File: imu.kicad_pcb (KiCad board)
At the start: 2 copper layers, 32.3 x 28.4 mm, 21 parts, among them J1 Conn_01x06, U1 LSM6DSL, U2 LIS2MDL, U3 AMS1117-3.3

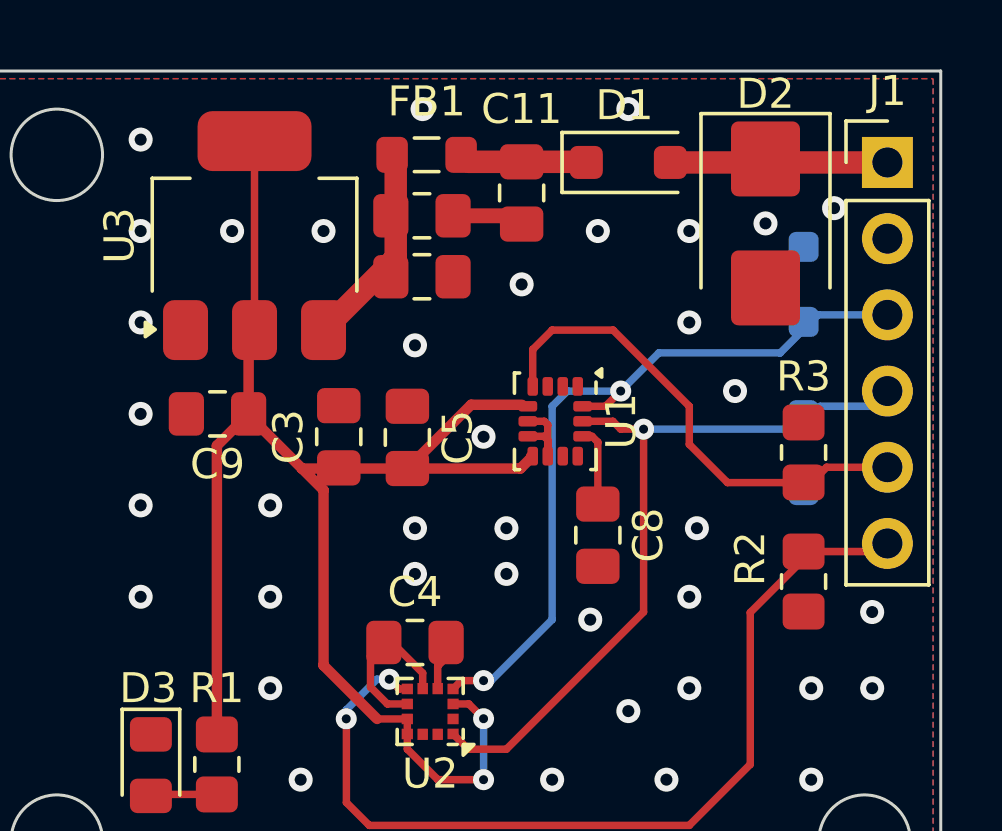
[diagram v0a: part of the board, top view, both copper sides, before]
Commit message: Add Fabrication Outputs
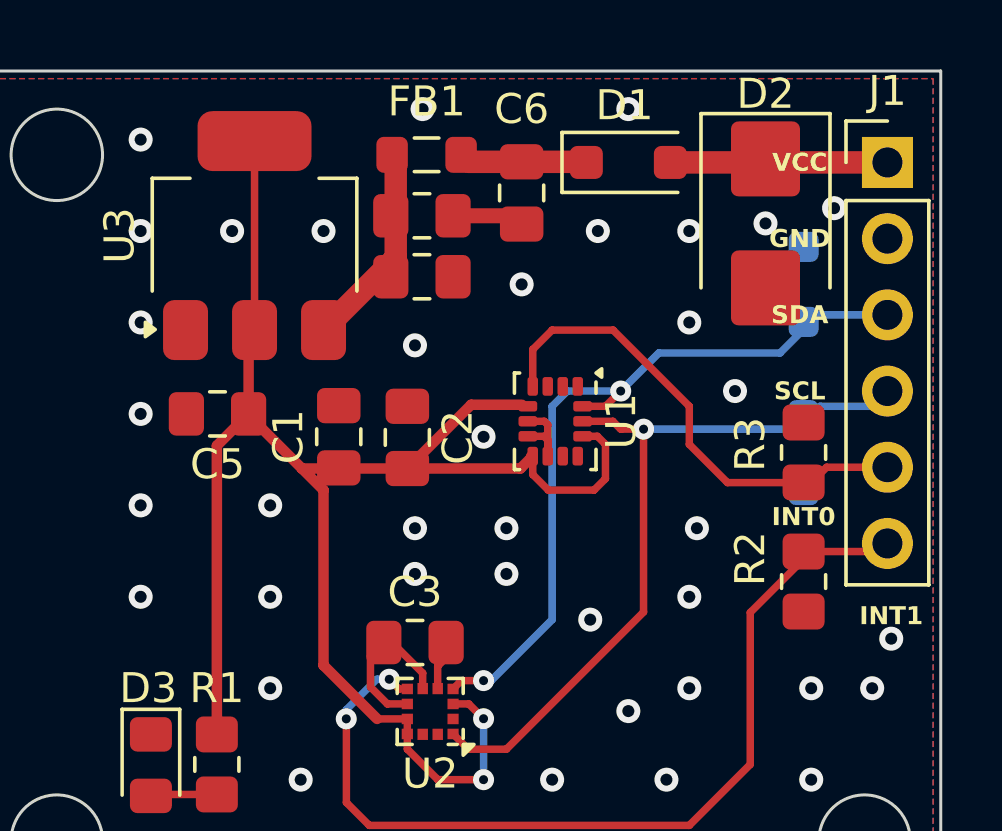
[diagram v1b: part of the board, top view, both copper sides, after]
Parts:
- removed C8: 200nF, Capacitor_SMD:C_0805_2012Metric_Pad1.18x1.45mm_HandSolder
- C3: renamed from C4; value 200nF -> 220nF
- renumbered C3 to C1, C5 to C2, C10 to C4, C9 to C5, C11 to C6, C12 to C7
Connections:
- U1 pad 12: Net-(U1-CS) -> +3V3
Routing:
- net +3V3: track 52.7 -> 58.2 mm
- net Net-(U1-CS): track 2.65 -> 0.00 mm
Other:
- board text added: "GND"
- board text added: "INT0"
- board text added: "INT1"
- board text added: "SCL"
- board text added: "SDA"
- board text added: "VCC"

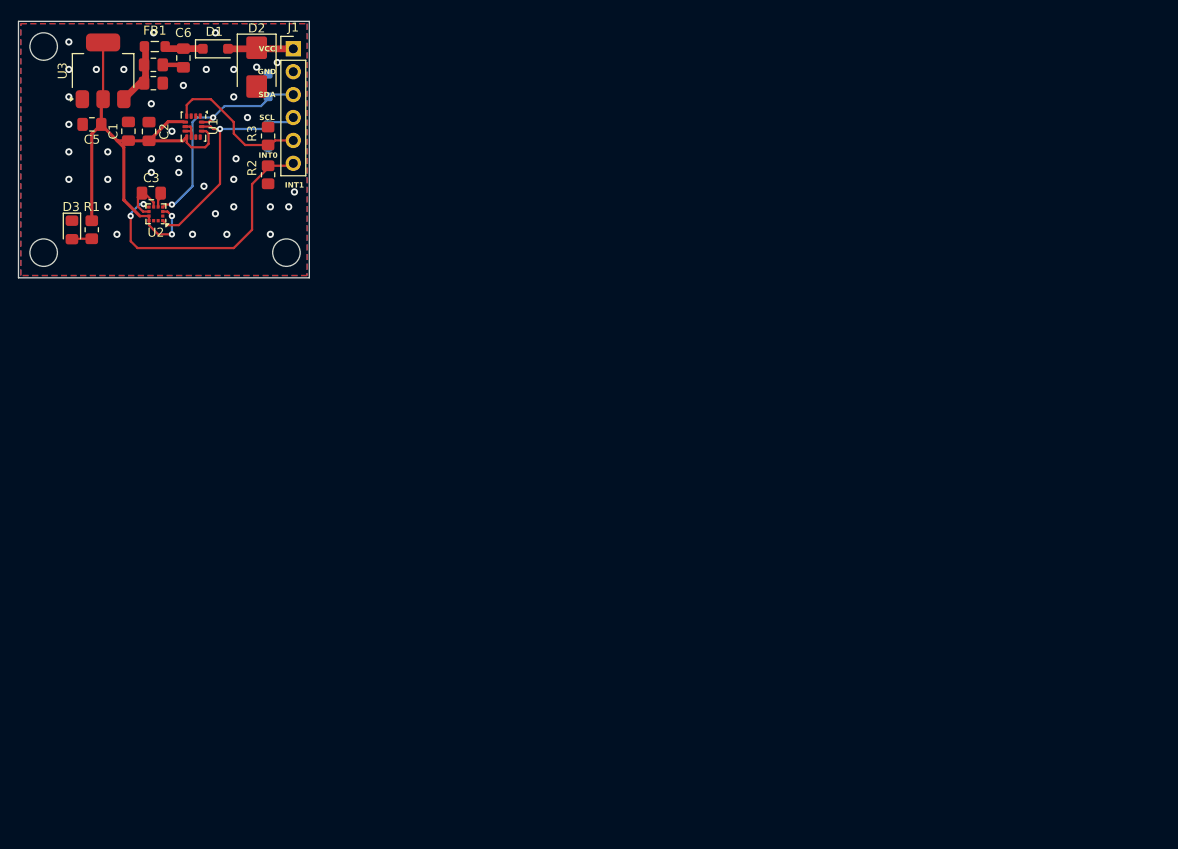
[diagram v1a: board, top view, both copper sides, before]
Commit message: Add Hierarchal Schematic + JST Connectors + GPIO
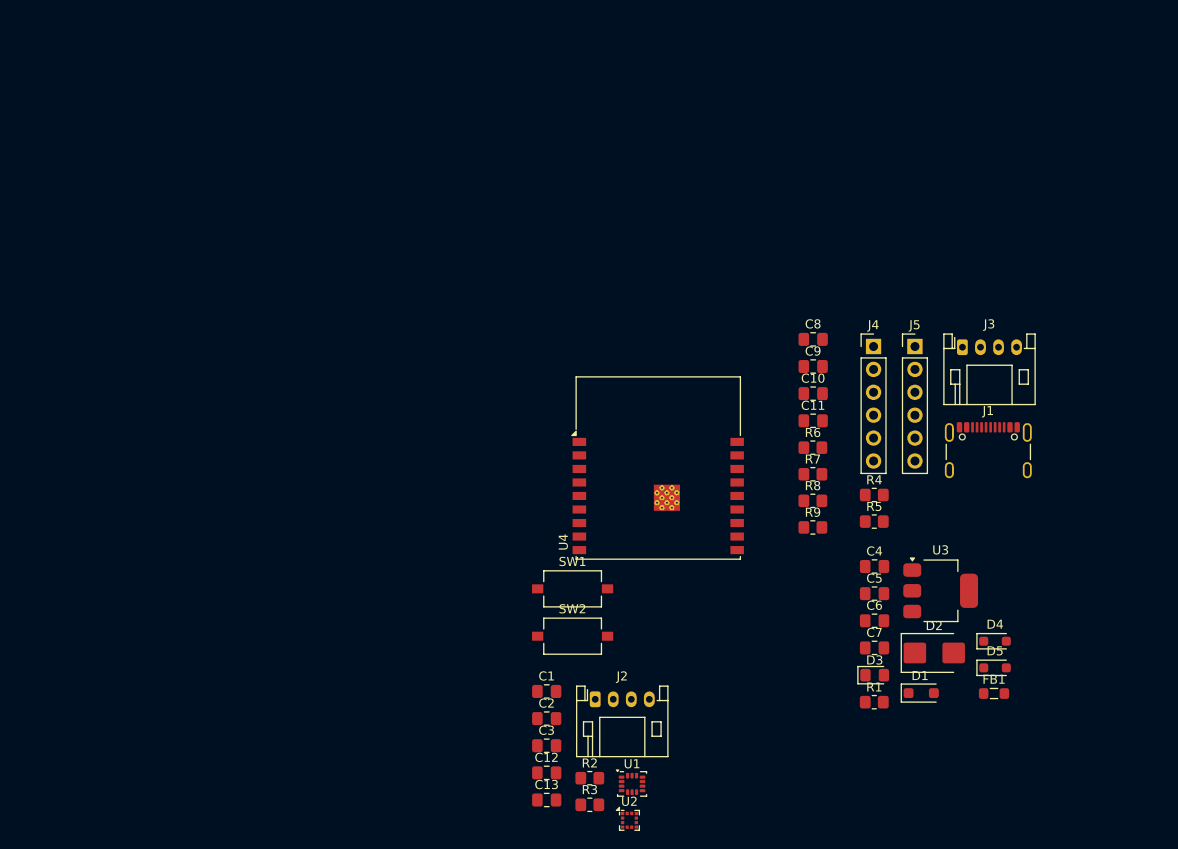
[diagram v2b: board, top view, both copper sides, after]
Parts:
- added C10: 1uF, Capacitor_SMD:C_0805_2012Metric_Pad1.18x1.45mm_HandSolder, F.Cu at (147.6, 60.1)
- added C11: 100nF, Capacitor_SMD:C_0805_2012Metric_Pad1.18x1.45mm_HandSolder, F.Cu at (147.6, 63.1)
- added C12: 10uF, Capacitor_SMD:C_0805_2012Metric_Pad1.18x1.45mm_HandSolder, F.Cu at (118.0, 102.2)
- added C13: 100nF, Capacitor_SMD:C_0805_2012Metric_Pad1.18x1.45mm_HandSolder, F.Cu at (118.0, 105.2)
- added C8: 100nF, Capacitor_SMD:C_0805_2012Metric_Pad1.18x1.45mm_HandSolder, F.Cu at (147.6, 54.1)
- added C9: 22uF, Capacitor_SMD:C_0805_2012Metric_Pad1.18x1.45mm_HandSolder, F.Cu at (147.6, 57.1)
- added J2: JST_PH2.0_01x04, Connector_JST:JST_PH_S4B-PH-K_1x04_P2.00mm_Horizontal, F.Cu at (123.4, 94.0)
- added J3: JST_PH2.0_01x04, Connector_JST:JST_PH_S4B-PH-K_1x04_P2.00mm_Horizontal, F.Cu at (164.1, 54.9)
- added J4: GPIO0, Connector_PinHeader_2.54mm:PinHeader_1x06_P2.54mm_Vertical, F.Cu at (154.3, 54.9)
- added J5: GPIO1, Connector_PinHeader_2.54mm:PinHeader_1x06_P2.54mm_Vertical, F.Cu at (158.9, 54.9)
- added R4: 5.1kR, Resistor_SMD:R_0805_2012Metric_Pad1.20x1.40mm_HandSolder, F.Cu at (154.4, 71.3)
- added R5: 5.1kR, Resistor_SMD:R_0805_2012Metric_Pad1.20x1.40mm_HandSolder, F.Cu at (154.4, 74.3)
- added R6: 10kR, Resistor_SMD:R_0805_2012Metric_Pad1.20x1.40mm_HandSolder, F.Cu at (147.5, 66.1)
- added R7: 100R, Resistor_SMD:R_0805_2012Metric_Pad1.20x1.40mm_HandSolder, F.Cu at (147.5, 69.0)
- added R8: 2.2kR, Resistor_SMD:R_0805_2012Metric_Pad1.20x1.40mm_HandSolder, F.Cu at (147.5, 72.0)
- added R9: 2.2kR, Resistor_SMD:R_0805_2012Metric_Pad1.20x1.40mm_HandSolder, F.Cu at (147.5, 74.9)
- added SW1: SW_Push, Button_Switch_SMD:SW_Tactile_SPST_NO_Straight_CK_PTS636Sx25SMTRLFS, F.Cu at (120.9, 81.7)
- added SW2: SW_Push, Button_Switch_SMD:SW_Tactile_SPST_NO_Straight_CK_PTS636Sx25SMTRLFS, F.Cu at (120.9, 87.0)
- added U4: ESP32-C3-WROOM-02, RF_Module:ESP32-C3-WROOM-02, F.Cu at (130.4, 71.4)
- D4, D5: moved to F.Cu
- J1: value Conn_01x06 -> USB_C_Receptacle_USB2.0_16P; footprint Connector_PinHeader_2.54mm:PinHeader_1x06_P2.54mm_Vertical -> Connector_USB:USB_C_Receptacle_GCT_USB4105-xx-A_16P_TopMnt_Horizontal
- moved FB1 117.5 mm to (167.6, 93.3), turned to 0 degrees
- moved U3 109.3 mm to (161.7, 82.0), turned to 0 degrees
- moved D1 106.0 mm to (159.6, 93.3)
- moved D5 103.3 mm to (167.8, 90.5), turned to 0 degrees
- moved C7 102.9 mm to (154.4, 88.3), turned to 0 degrees
- moved D3 101.8 mm to (154.4, 91.3), turned to 0 degrees
- moved R1 101.4 mm to (154.4, 94.3), turned to 0 degrees
- moved C5 101.2 mm to (154.4, 82.3), turned to 0 degrees
- moved D2 99.3 mm to (161.0, 88.8), turned to 0 degrees
- moved C6 98.9 mm to (154.4, 85.3), turned to 0 degrees
- moved D4 98.2 mm to (167.8, 87.5), turned to 0 degrees
- moved C4 96.3 mm to (154.4, 79.3)
- moved J1 89.6 mm to (167.0, 67.5)
- moved U1 87.6 mm to (127.5, 103.4), turned to 0 degrees
- moved U2 85.3 mm to (127.2, 107.4), turned to 0 degrees
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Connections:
- C4 pad 1: VCC -> +5V
- C7 pad 2: VCC -> +5V
- D1 pad 2: Net-(D1-A) -> +5V
- D2 pad 1: Net-(D1-A) -> GND
- D2 pad 2: GND -> +5V
- D5 pad 2: SDA -> SCL
- FB1 pad 2: VCC -> +5V
- R2 pad 1: INT1 -> INT_MAG
- R3 pad 1: INT0 -> INT_IMU
- U1 pad 14: SDA -> SCL
- U1 pad 4: INT0 -> INT_IMU
- U2 pad 4: SDA -> SCL
- U2 pad 7: INT1 -> INT_MAG
- U3 pad 3: VCC -> +5V
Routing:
- net +3V3: track 58.2 -> 0.00 mm, vias 2 -> 0
- net INT1: track 30.9 -> 0.00 mm, vias 2 -> 0
- net SCL: track 25.3 -> 0.00 mm, vias 1 -> 0
- net SDA: track 25.3 -> 0.00 mm, vias 2 -> 0
- net INT0: track 16.4 -> 0.00 mm
- net GND: track 10.2 -> 0.00 mm, vias 38 -> 0
- net Net-(D1-A): track 7.24 -> 0.00 mm
- net VCC: track 6.58 -> 0.00 mm
- net Net-(D1-K): track 4.28 -> 0.00 mm
- net Net-(D3-A): track 2.22 -> 0.00 mm
- net Net-(U2-C1): track 1.65 -> 0.00 mm
- removed copper zone on B.Cu, net GND
- removed copper zone on F.Cu, net GND
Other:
- board outline removed
- board text removed: "GND"
- board text removed: "INT0"
- board text removed: "INT1"
- board text removed: "SCL"
- board text removed: "SDA"
- board text removed: "VCC"

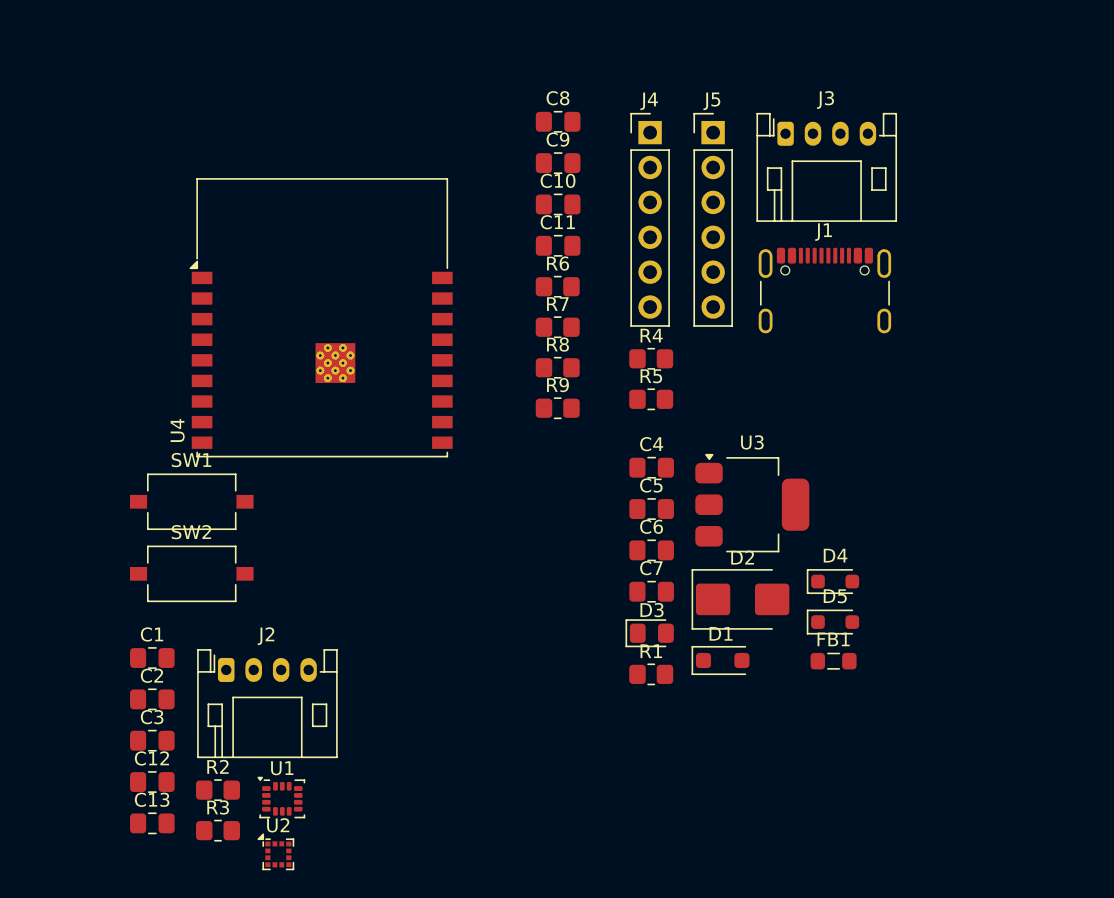
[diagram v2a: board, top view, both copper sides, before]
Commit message: Route Traces for ESP32 and related IO
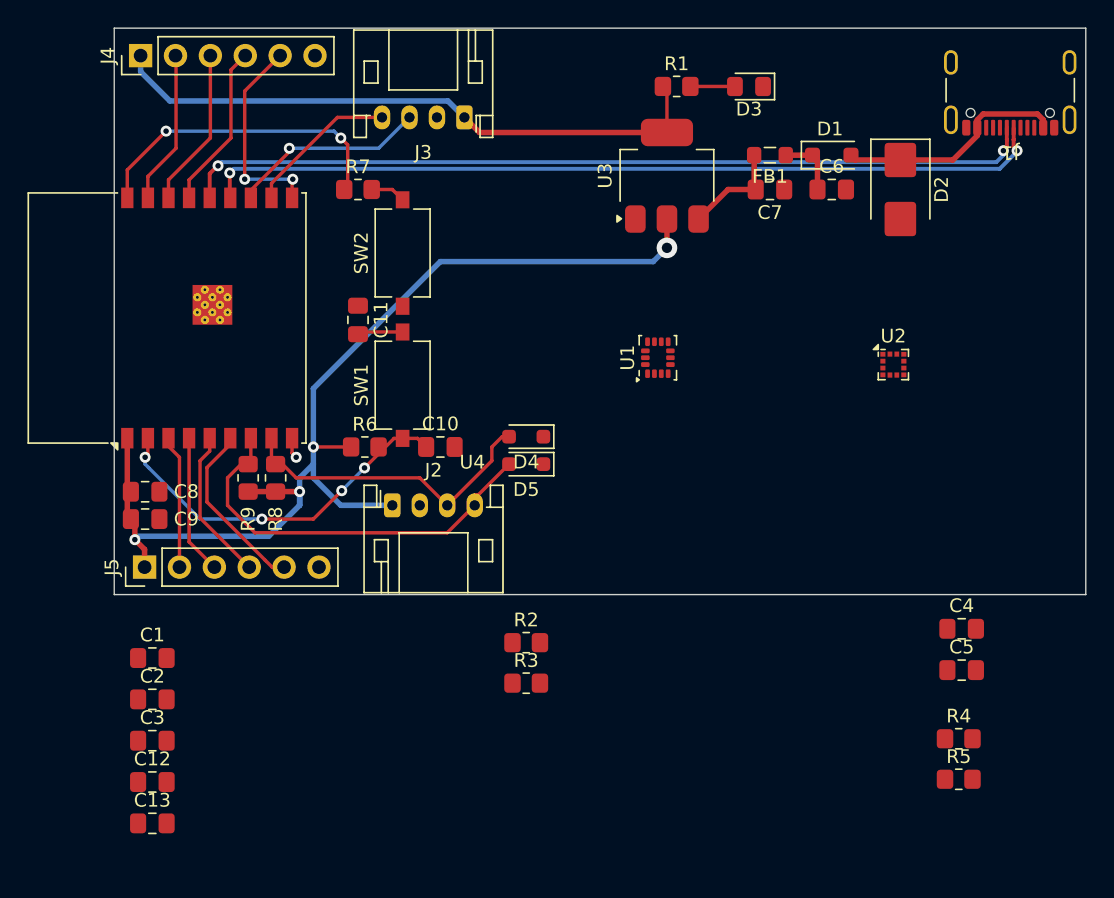
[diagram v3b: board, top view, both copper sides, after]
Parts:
- moved U2 57.3 mm to (172.0, 71.8)
- moved J5 52.1 mm to (117.5, 86.5), turned to 90 degrees
- moved R1 42.9 mm to (156.2, 51.5)
- moved U1 42.2 mm to (154.8, 71.2), turned to 90 degrees
- moved D3 40.4 mm to (161.5, 51.5), turned to 180 degrees
- moved C8 40.4 mm to (117.5, 81.0), turned to 180 degrees
- moved C9 39.7 mm to (117.5, 83.0), turned to 180 degrees
- moved D1 37.6 mm to (167.5, 56.5)
- moved J4 37.5 mm to (117.2, 49.2), turned to 90 degrees
- moved FB1 37.1 mm to (163.0, 56.5), turned to 180 degrees
- moved R4 35.6 mm to (176.8, 99.0)
- moved R5 35.6 mm to (176.8, 102.0)
- moved D2 32.0 mm to (172.5, 59.0), turned to -90 degrees
- moved C7 30.5 mm to (163.0, 59.0), turned to 180 degrees
- moved C6 29.4 mm to (167.5, 59.0)
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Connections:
- C8 pad 2: +3.3V -> +3V3
- C9 pad 2: +3.3V -> +3V3
- D2 pad 1: GND -> +5V
- D2 pad 2: +5V -> GND
- D5 pad 2: SCL -> SDA
- J2 pad 1: +3.3V -> +3V3
- J2 pad 4: SCL -> SDA
- J4 pad 1: +3.3V -> +3V3
- J4 pad 2: IO0 -> IO1
- J4 pad 3: IO1 -> IO2
- J4 pad 4: IO2 -> IO3
- J4 pad 5: IO3 -> IO8
- J5 pad 1: +3.3V -> +3V3
- R6 pad 1: +3.3V -> +3V3
- R8 pad 1: +3.3V -> +3V3
- R9 pad 1: +3.3V -> +3V3
- R9 pad 2: SCL -> SDA
- U1 pad 14: SCL -> SDA
- U2 pad 4: SCL -> SDA
- U4 pad 1: +3.3V -> +3V3
- U4 pad 10: unconnected-(U4-IO10-Pad10) -> IO8
- U4 pad 18: IO0 -> BOOT
- U4 pad 7: SCL -> SDA
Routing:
- net +3V3: track 0.00 -> 124.0 mm, vias 0 -> 4
- net USB_D-: track 0.00 -> 62.5 mm, vias 0 -> 2
- net USB_D+: track 0.00 -> 61.7 mm, vias 0 -> 2
- net SDA: track 0.00 -> 29.7 mm
- net EN: track 0.00 -> 26.8 mm, vias 0 -> 4
- net +5V: track 0.00 -> 24.6 mm
- net BOOT: track 0.00 -> 23.0 mm, vias 0 -> 2
- net SCL: track 0.00 -> 22.9 mm
- net IO8: track 0.00 -> 14.9 mm, vias 0 -> 2
- net TX0: track 0.00 -> 14.5 mm, vias 0 -> 1
- net IO7: track 0.00 -> 12.9 mm
- net IO3: track 0.00 -> 12.1 mm
- net IO2: track 0.00 -> 11.6 mm
- net IO1: track 0.00 -> 11.2 mm
- net IO6: track 0.00 -> 11.2 mm
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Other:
- board outline added: 70.8 x 41.2 mm
- copper layers 2 -> 4
